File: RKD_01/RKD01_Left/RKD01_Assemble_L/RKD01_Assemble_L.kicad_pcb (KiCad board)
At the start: 2 copper layers, 164.3 x 126.2 mm, 82 parts, among them J1 TRRS, M1 Mark, M10 Mark, M2 Mark, M3 Mark, M4 Mark, M5 Mark, M6 Mark, M7 Mark, M8 Mark, M9 Mark, SW1 SW_Push, SW10 SW_Push, SW11 SW_Push, SW12 SW_Push, SW13 SW_Push, SW14 SW_Push, SW15 SW_Push, SW16 SW_Push, SW17 SW_Push, SW18 SW_Push, SW19 SW_Push, SW2 SW_Push, SW20 SW_Push, SW21 SW_Push, SW22 SW_Push, SW23 SW_Push, SW24 SW_Push, SW25 SW_Push, SW26 SW_Push, SW27 SW_Push, SW28 SW_Push, SW29 SW_Push, SW3 SW_Push, SW30 SW_Push, SW31 SW_Push, SW32 SW_Push, SW33 SW_Push, SW34 RotaryEncoder_Switch, SW35 SW_Push, SW4 SW_Push, SW5 SW_Push, SW6 SW_Push, SW7 SW_Push, SW8 SW_Push, SW9 SW_Push, U1 ProMicro

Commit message: ロータリーエンコーダを諦め
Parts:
- SW34: value RotaryEncoder_Switch -> SW_Push; footprint BrownSugar_KBD:RotaryEncoder_EC11-Switch -> kbd_SW:Choc_Hotswap_1u
- moved D34 2.38 mm to (161.9, 128.6)
- turned SW34 to 0 degrees
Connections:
- U1 pad 12: REA -> unconnected-(U1-B5/9-Pad12)
- U1 pad 13: REB -> unconnected-(U1-10/B6-Pad13)
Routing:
- net REA: track 229.1 -> 0.00 mm, vias 1 -> 0
- net REB: track 214.3 -> 0.00 mm, vias 1 -> 0
- net GND: track 264.3 -> 63.6 mm, vias 1 -> 0
- net Col1: track 134.6 -> 123.5 mm
- net Col6: track 204.1 -> 208.6 mm
- net Col3: track 161.0 -> 158.5 mm
- net Row4: track 249.6 -> 252.0 mm
- net Net-(D25-A): track 18.2 -> 20.2 mm
- net Net-(D4-A): track 18.9 -> 20.8 mm
- net Col0: track 109.7 -> 107.8 mm
- net Col2: track 142.6 -> 140.7 mm
- net Col4: track 176.0 -> 174.2 mm
- net Col5: track 165.6 -> 164.1 mm
- net Net-(D34-A): track 8.37 -> 7.17 mm
- net Row2: track 203.2 -> 202.4 mm
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
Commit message: 寸法を見直し
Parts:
- moved M7 21.4 mm to (26.2, 140.5)
- moved M2 4.76 mm to (185.7, 23.8)
- moved M8 4.76 mm to (185.7, 140.5)
- moved D15 2.38 mm to (76.2, 128.6)
- moved D20 2.38 mm to (100.0, 128.6)
- moved D22 2.38 mm to (111.9, 71.4)
- moved D25 2.38 mm to (123.8, 128.6)
- moved D28 2.38 mm to (135.7, 90.5)
- moved D31 2.38 mm to (150.0, 71.4)
- moved D33 2.38 mm to (159.5, 109.5)
- moved M4 2.38 mm to (135.7, 47.6)
- moved M6 2.38 mm to (135.7, 104.8)
- moved SW13 2.38 mm to (88.1, 95.2)
- moved SW19 2.38 mm to (111.9, 114.3)
- moved SW21 2.38 mm to (111.9, 57.1)
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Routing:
- net Col1: track 123.5 -> 137.1 mm
- net Col4: track 174.2 -> 186.7 mm
- net Col5: track 164.1 -> 172.0 mm
- net Col6: track 208.6 -> 213.8 mm
- net Col2: track 140.7 -> 144.2 mm
- net Col3: track 158.5 -> 161.0 mm
- net Col0: track 107.8 -> 110.0 mm
- net Row3: track 244.5 -> 246.5 mm
- net Row2: track 202.4 -> 204.1 mm
- net Row4: track 252.0 -> 250.7 mm
- net Row1: track 188.0 -> 187.0 mm
- net Net-(D25-A): track 20.2 -> 21.1 mm
- net Net-(D4-A): track 20.8 -> 21.7 mm
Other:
- board size 164.3 x 126.2 mm -> 169.1 x 126.2 mm

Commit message: デザイン見直し
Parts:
- removed the M5 at (73.8, 85.7)
- removed the M6 at (135.7, 104.8)
- removed M7, M8: Mark, kbd_Hole:m2_Spacer_Hole_hex
- removed OL1: OLED, BrownSugar_KBD:OLED_center_module
- removed SW35: SW_Push, kbd_Parts:ResetSW
- moved M4 109.0 mm to (192.9, 140.5)
- moved M3 93.0 mm to (26.2, 140.5)
- moved M2 7.14 mm to (192.9, 23.8)
- moved D27 4.76 mm to (135.7, 71.4)
- moved D29 4.76 mm to (145.3, 109.5)
- moved D30 4.76 mm to (145.3, 52.4)
- moved D32 4.76 mm to (159.5, 90.5)
- moved D34 4.76 mm to (169.1, 128.6)
- moved SW24 4.76 mm to (135.7, 114.3)
- moved SW26 4.76 mm to (135.7, 57.1)
- moved SW27 4.76 mm to (145.3, 76.2)
- moved SW32 4.76 mm to (169.1, 95.2)
- moved D10 4.76 mm to (57.2, 128.6)
- moved D12 4.76 mm to (78.6, 71.4)
- moved D13 4.76 mm to (83.3, 90.5)
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- renumbered M9 to M5, M10 to M6
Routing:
- net Reset: track 34.4 -> 0.00 mm
- net Row3: track 246.5 -> 232.2 mm, vias 0 -> 1
- net Col5: track 172.0 -> 183.0 mm
- net Col2: track 144.2 -> 153.4 mm
- net SDA: track 44.2 -> 35.1 mm
- net SCL: track 39.9 -> 31.6 mm, vias 1 -> 0
- net Col6: track 213.8 -> 220.7 mm
- net GND: track 63.6 -> 57.8 mm
- net VCC: track 65.3 -> 60.1 mm, vias 1 -> 0
- net Col3: track 161.0 -> 166.1 mm
- net Row1: track 187.0 -> 182.1 mm
- net Row0: track 159.0 -> 161.7 mm
- net Col0: track 110.0 -> 112.7 mm
- net Row2: track 204.1 -> 201.9 mm
- net Col4: track 186.7 -> 188.6 mm
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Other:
- board size 169.1 x 126.2 mm -> 176.2 x 126.2 mm

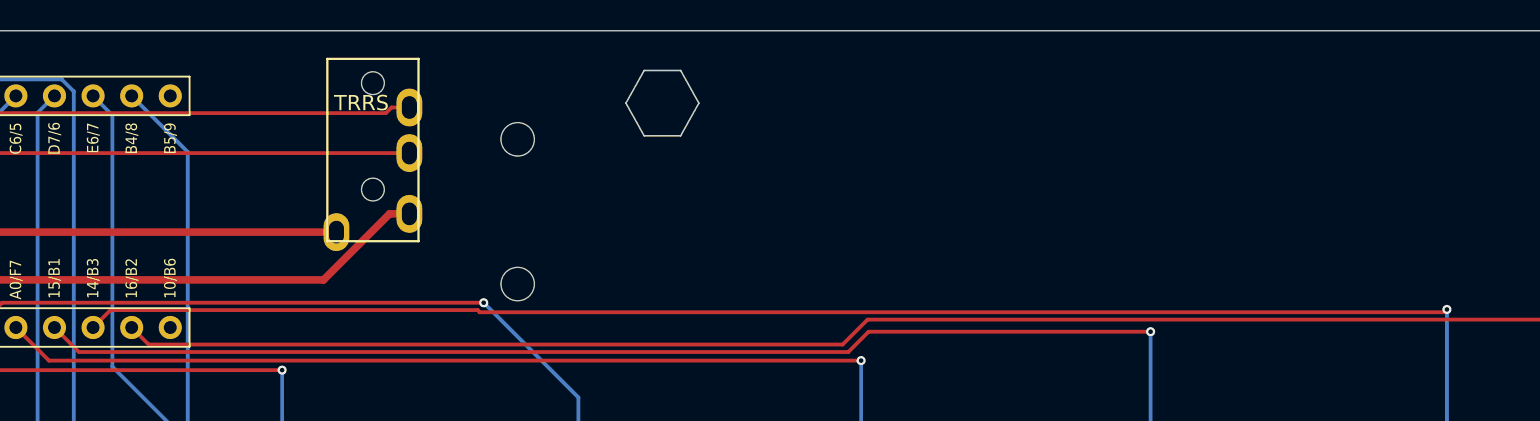
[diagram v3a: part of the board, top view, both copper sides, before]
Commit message: promicro部分拡張
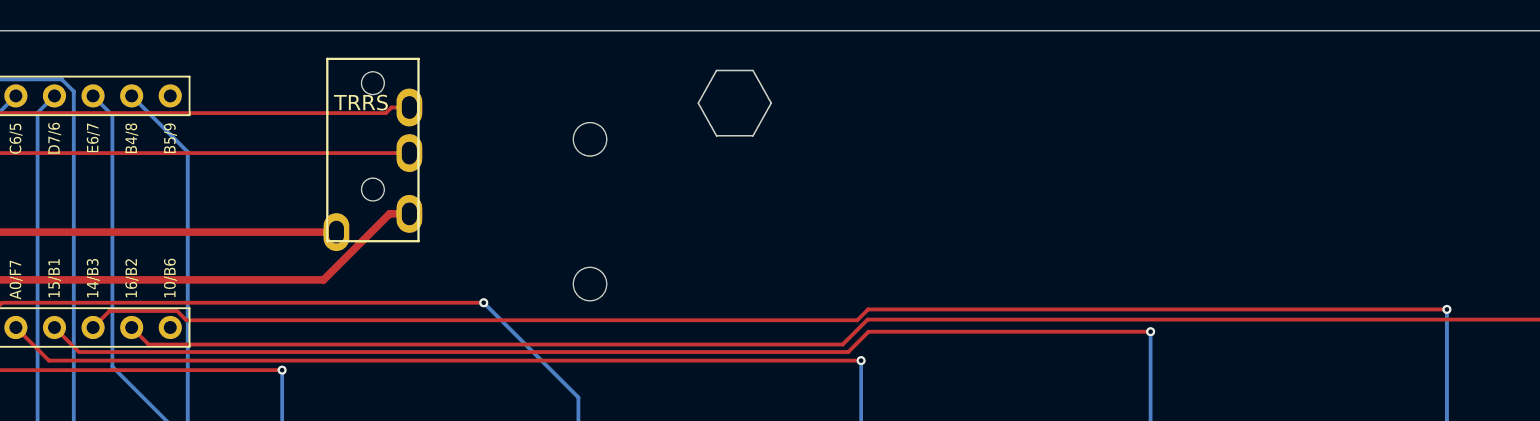
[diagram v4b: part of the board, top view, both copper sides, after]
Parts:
- moved M1 4.76 mm to (92.9, 23.8)
- moved M5 4.76 mm to (83.3, 26.2)
- moved M6 4.76 mm to (83.3, 35.7)
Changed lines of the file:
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@@
 	(footprint "kbd_Hole:m2_Screw_Hole"
 		(layer "F.Cu")
-		(at 78.5813 26.1937)
+		(at 83.34375 26.1937)
 		(descr "Mounting Hole 2.2mm, no annular, M2")
 		(tags "mounting hole 2.2mm no annular m2")
@@
 	(footprint "kbd_Hole:m2_Screw_Hole"
 		(layer "F.Cu")
-		(at 78.5813 35.7187)
+		(at 83.34375 35.7187)
 		(descr "Mounting Hole 2.2mm, no annular, M2")
 		(tags "mounting hole 2.2mm no annular m2")
@@
 	(footprint "kbd_Hole:m2_Spacer_Hole_hex"
 		(layer "F.Cu")
-		(at 88.1063 23.8125)
+		(at 92.86875 23.8125)
 		(descr "Mounting Hole 2.2mm, no annular, M2")
 		(tags "mounting hole 2.2mm no annular m2")
@@
 	(gr_line
 		(start 21.43115 42.86255)
-		(end 80.9624 42.86255)
+		(end 85.72485 42.86255)
 		(stroke
 			(width 0.1)
@@
 	)
 	(gr_line
-		(start 83.3437 45.24375)
-		(end 83.3437 19.05)
+		(start 88.10615 45.24375)
+		(end 88.10615 19.05)
 		(stroke
 			(width 0.1)
@@
 	(gr_line
 		(start 23.8125 45.24375)
-		(end 83.3437 45.24375)
+		(end 88.10615 45.24375)
 		(stroke
 			(width 0.1)
@@
 	)
 	(gr_line
-		(start 80.9624 42.86255)
-		(end 80.9624 19.05005)
+		(start 85.72485 42.86255)
+		(end 85.72485 19.05005)
 		(stroke
 			(width 0.1)
@@
 	)
 	(segment
-		(start 139.5461 37.5729)
+		(start 56.782351 38.1)
+		(end 100.930004 38.1)
+		(width 0.25)
+		(layer "F.Cu")
+		(net 49)
+	)
+	(segment
+		(start 101.642304 37.3877)
 		(end 139.7313 37.3877)
 		(width 0.25)
@@
 	)
 	(segment
-		(start 76.0873 37.5729)
-		(end 139.5461 37.5729)
+		(start 51.7283 37.4892)
+		(end 56.171551 37.4892)
 		(width 0.25)
 		(layer "F.Cu")
@@
 	(segment
 		(start 50.6413 38.5762)
-		(end 51.7871 37.4304)
+		(end 51.7283 37.4892)
 		(width 0.25)
 		(layer "F.Cu")
@@
 	)
 	(segment
-		(start 51.7871 37.4304)
-		(end 75.9448 37.4304)
+		(start 100.930004 38.1)
+		(end 101.642304 37.3877)
 		(width 0.25)
 		(layer "F.Cu")
@@
 	)
 	(segment
-		(start 75.9448 37.4304)
-		(end 76.0873 37.5729)
+		(start 56.171551 37.4892)
+		(end 56.782351 38.1)
 		(width 0.25)
 		(layer "F.Cu")

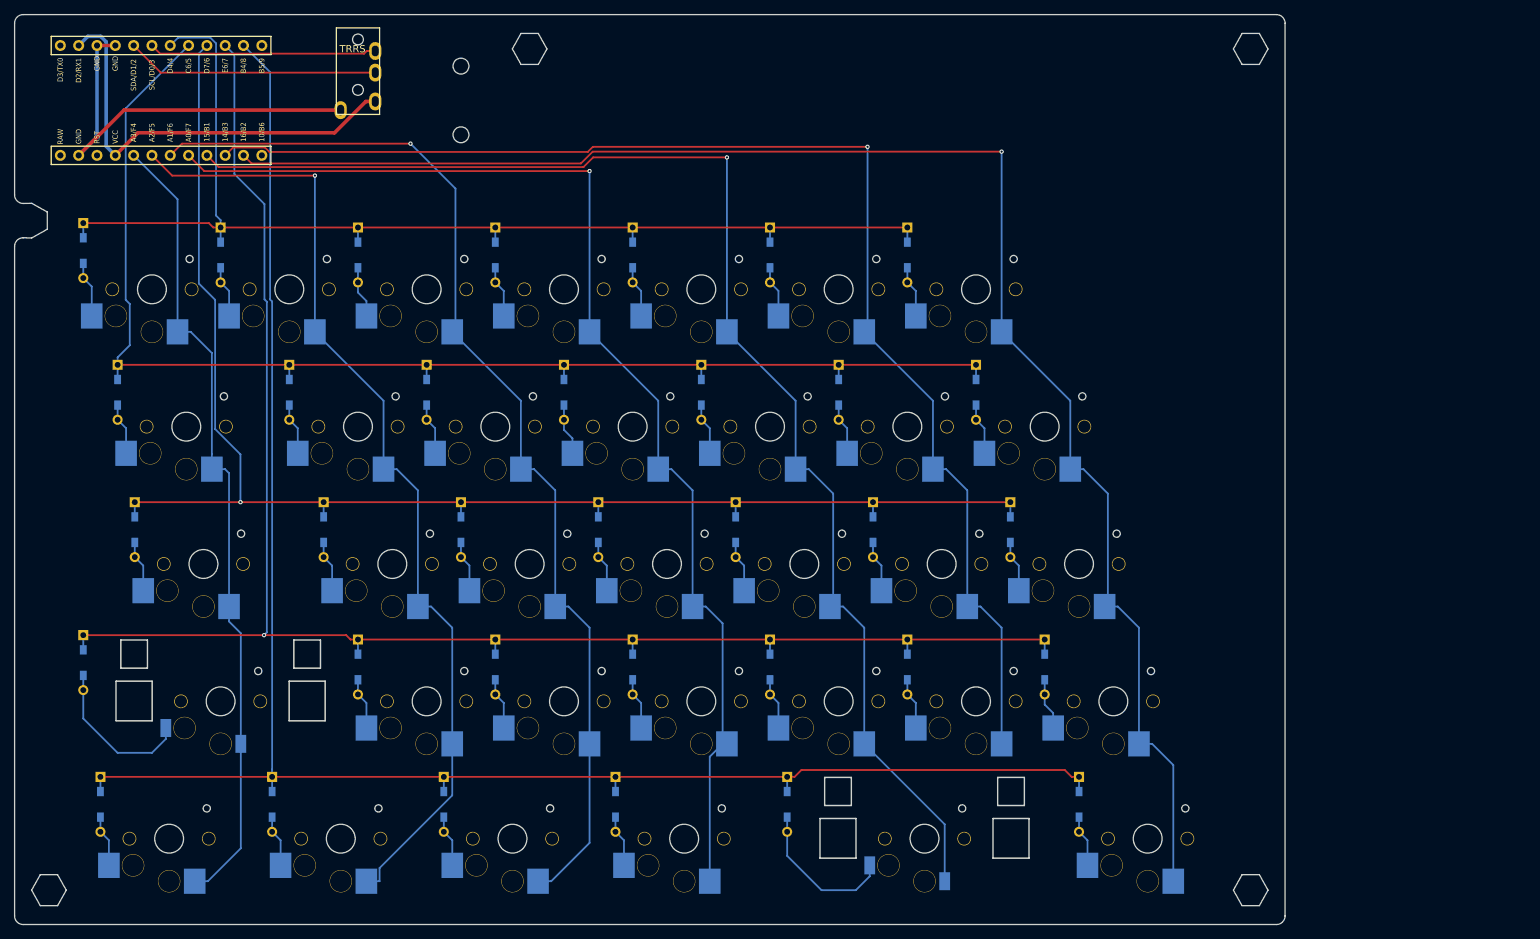
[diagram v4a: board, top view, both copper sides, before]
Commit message: 左一列追加Assemble
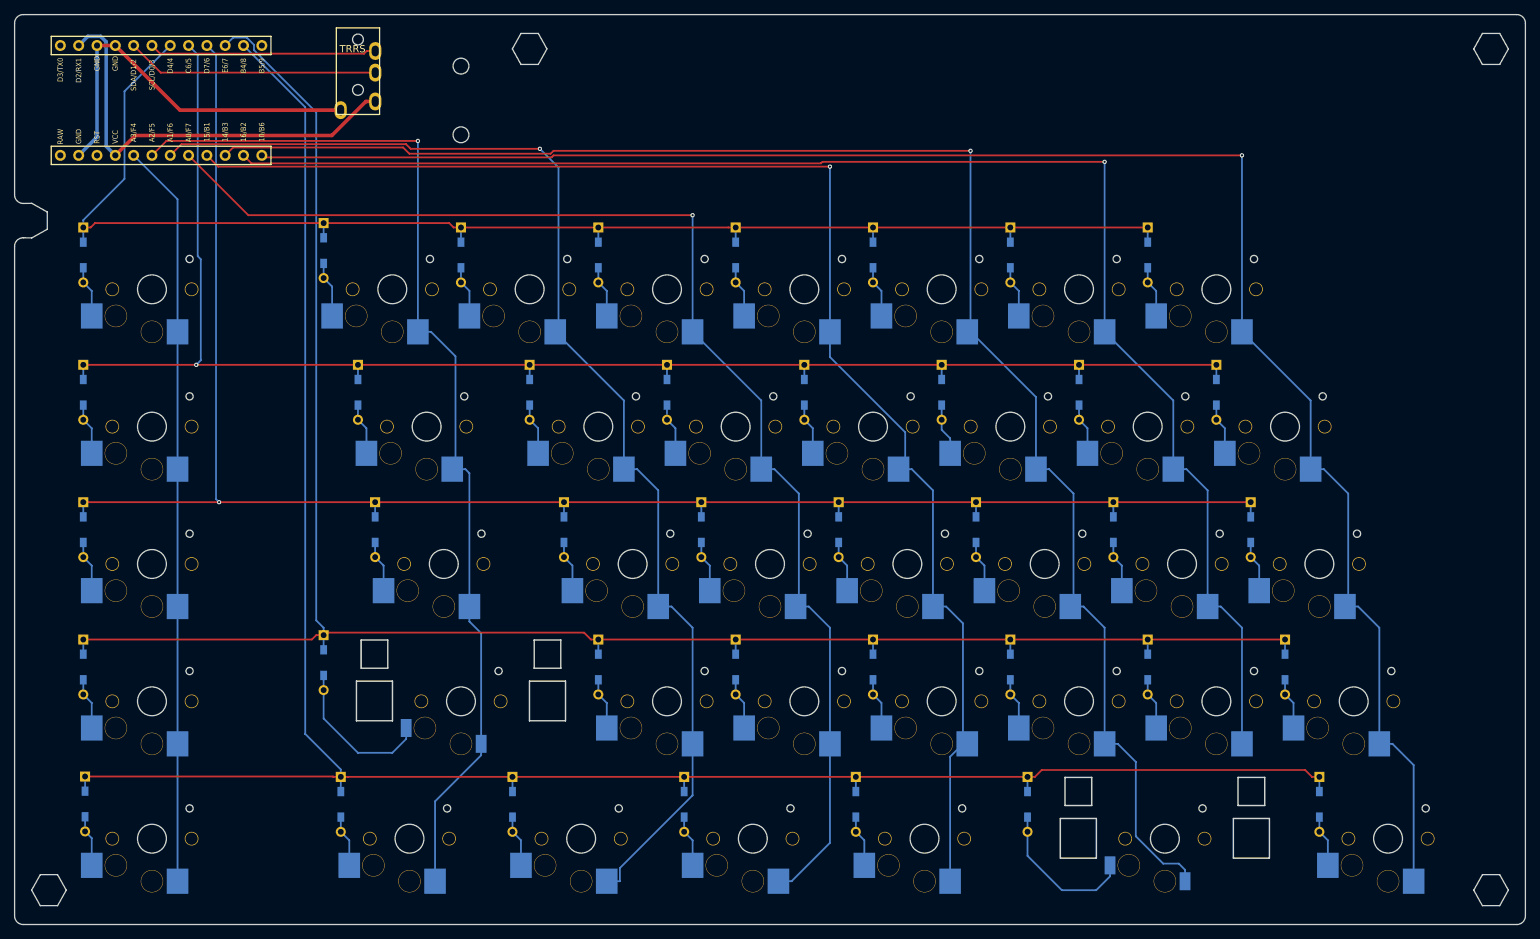
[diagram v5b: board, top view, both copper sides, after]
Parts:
- added D1: D, kbd_Parts:Diode_TH_SMD, F.Cu at (31.0, 52.4)
- added D2: D, kbd_Parts:Diode_TH_SMD, F.Cu at (31.0, 71.4)
- added D3: D, kbd_Parts:Diode_TH_SMD, F.Cu at (31.0, 90.5)
- added D4: D, kbd_Parts:Diode_TH_SMD, F.Cu at (31.0, 109.5)
- added D5: D, kbd_Parts:Diode_TH_SMD, F.Cu at (31.2, 128.5)
- added SW1: SW_Push, kbd_SW:Choc_Hotswap_1u, F.Cu at (40.5, 57.1)
- added SW2: SW_Push, kbd_SW:Choc_Hotswap_1u, F.Cu at (40.5, 76.2)
- added SW3: SW_Push, kbd_SW:Choc_Hotswap_1u, F.Cu at (40.5, 95.2)
- added SW4: SW_Push, kbd_SW:Choc_Hotswap_1u, F.Cu at (40.5, 114.3)
- added SW5: SW_Push, kbd_SW:Choc_Hotswap_1u, F.Cu at (40.5, 133.3)
- moved M2 33.3 mm to (226.2, 23.8)
- moved M4 33.3 mm to (226.2, 140.5)
- moved D14 33.3 mm to (102.4, 109.5)
- moved D16 33.3 mm to (102.4, 52.4)
- moved D17 33.3 mm to (111.9, 71.4)
- moved D20 33.3 mm to (114.3, 128.6)
- moved D23 33.3 mm to (135.7, 90.5)
- moved D27 33.3 mm to (150.0, 71.4)
- moved D29 33.3 mm to (159.5, 109.5)
- moved D31 33.3 mm to (159.5, 52.4)
- moved D32 33.3 mm to (169.1, 71.4)
- moved D33 33.3 mm to (173.8, 90.5)
- moved D36 33.3 mm to (188.1, 71.4)
- moved D37 33.3 mm to (192.9, 90.5)
- moved D38 33.3 mm to (197.6, 109.5)
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- renumbered D5 to D10, D6 to D11, D7 to D12, D8 to D13, D9 to D14, D10 to D15, D11 to D16, D12 to D17, D13 to D18, D14 to D19, D15 to D20, D16 to D21, D17 to D22, D18 to D23, D19 to D24, D20 to D25, D21 to D26, D22 to D27, D23 to D28, D24 to D29, D25 to D30, D26 to D31, D27 to D32, D28 to D33, D29 to D34, D30 to D35, D31 to D36, D32 to D37, D33 to D38, D34 to D39, D1 to D6, D2 to D7, D3 to D8, D4 to D9, SW5 to SW10, SW6 to SW11, SW7 to SW12, SW8 to SW13, SW9 to SW14, SW10 to SW15, SW11 to SW16, SW12 to SW17, SW13 to SW18, SW14 to SW19, SW15 to SW20, SW16 to SW21, SW17 to SW22, SW18 to SW23, SW19 to SW24, SW20 to SW25, SW21 to SW26, SW22 to SW27, SW23 to SW28, SW24 to SW29, SW25 to SW30, SW26 to SW31, SW27 to SW32, SW28 to SW33, SW29 to SW34, SW30 to SW35, SW31 to SW36, SW32 to SW37, SW33 to SW38, SW34 to SW39, SW1 to SW6, SW2 to SW7, SW3 to SW8, SW4 to SW9
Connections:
- SW10 pad 2: Col0 -> Col1
- SW11 pad 2: Col1 -> Col2
- SW12 pad 2: Col1 -> Col2
- SW13 pad 2: Col1 -> Col2
- SW14 pad 2: Col1 -> Col2
- SW15 pad 2: Col1 -> Col2
- SW16 pad 2: Col2 -> Col3
- SW17 pad 2: Col2 -> Col3
- SW18 pad 2: Col2 -> Col3
- SW19 pad 2: Col2 -> Col3
- SW20 pad 2: Col2 -> Col3
- SW21 pad 2: Col3 -> Col4
- SW22 pad 2: Col3 -> Col4
- SW23 pad 2: Col3 -> Col4
- SW24 pad 2: Col3 -> Col4
- SW25 pad 2: Col3 -> Col4
- SW26 pad 2: Col4 -> Col5
- SW27 pad 2: Col4 -> Col5
- SW28 pad 2: Col4 -> Col5
- SW29 pad 2: Col4 -> Col5
- SW30 pad 2: Col4 -> Col5
- SW31 pad 2: Col5 -> Col6
- SW32 pad 2: Col5 -> Col6
- SW33 pad 2: Col5 -> Col6
- SW34 pad 2: Col5 -> Col6
- SW35 pad 2: Col6 -> Col7
- SW36 pad 2: Col6 -> Col7
- SW37 pad 2: Col6 -> Col7
- SW38 pad 2: Col6 -> Col7
- SW39 pad 2: Col6 -> Col7
- SW6 pad 2: Col0 -> Col1
- SW7 pad 2: Col0 -> Col1
- SW8 pad 2: Col0 -> Col1
- SW9 pad 2: Col0 -> Col1
- U1 pad 13: unconnected-(U1-10/B6-Pad13) -> Col7
- U1 pad 22: Reset -> unconnected-(U1-RST-Pad22)
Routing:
- net Col7: track 0.00 -> 250.1 mm, vias 0 -> 1
- net Row3: track 232.2 -> 274.5 mm, vias 1 -> 0
- net Row4: track 251.8 -> 293.3 mm
- net Row2: track 201.9 -> 242.2 mm
- net Col5: track 183.4 -> 223.1 mm
- net Row1: track 182.1 -> 218.7 mm, vias 0 -> 1
- net Row0: track 161.7 -> 194.7 mm
- net Col2: track 153.4 -> 171.3 mm
- net Col3: track 166.1 -> 180.0 mm
- net Col1: track 137.7 -> 149.0 mm
- net Col6: track 220.7 -> 210.7 mm
- net Col0: track 112.7 -> 103.2 mm
- net Col4: track 188.6 -> 197.7 mm
- net Net-(D4-A): track 0.00 -> 7.17 mm
- net Net-(D3-A): track 0.00 -> 7.17 mm
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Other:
- board size 176.2 x 126.2 mm -> 209.6 x 126.2 mm

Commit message: プロット出力
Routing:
- net Col5: track 223.1 -> 220.8 mm
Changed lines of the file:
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@@
-	)
-	(segment
-		(start 183.7751 139.25)
-		(end 183.7751 137.6733)
-		(width 0.25)
-		(layer "B.Cu")
-		(net 49)
-	)
-	(segment
-		(start 176.9436 122.6981)
-		(end 174.4455 120.2)
-		(width 0.25)
-		(layer "B.Cu")
-		(net 49)
 	)
 	(segment
@@
 	)
 	(segment
-		(start 176.9436 133.015)
-		(end 176.9436 122.6981)
+		(start 183.7751 131.3563)
+		(end 172.6188 120.2)
 		(width 0.25)
 		(layer "B.Cu")
@@
 	)
 	(segment
-		(start 183.7751 137.6733)
-		(end 182.911 136.8092)
-		(width 0.25)
-		(layer "B.Cu")
-		(net 49)
-	)
-	(segment
-		(start 172.6188 120.2)
-		(end 174.4455 120.2)
+		(start 183.7751 139.25)
+		(end 183.7751 131.3563)
 		(width 0.25)
 		(layer "B.Cu")
@@
 		(width 0.25)
 		(layer "B.Cu")
-		(net 49)
-	)
-	(segment
-		(start 180.7378 136.8092)
-		(end 176.9436 133.015)
-		(width 0.25)
-		(layer "B.Cu")
-		(net 49)
-	)
-	(segment
-		(start 182.911 136.8092)
-		(end 180.7378 136.8092)
-		(width 0.25)
-		(layer "B.Cu")
